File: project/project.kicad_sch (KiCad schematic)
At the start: 6 parts, among them J1 Conn_02x16_Odd_Even, J2 USB_C_Receptacle_PowerOnly_6P, SW1 SS-12D10L9, U2 CH224K

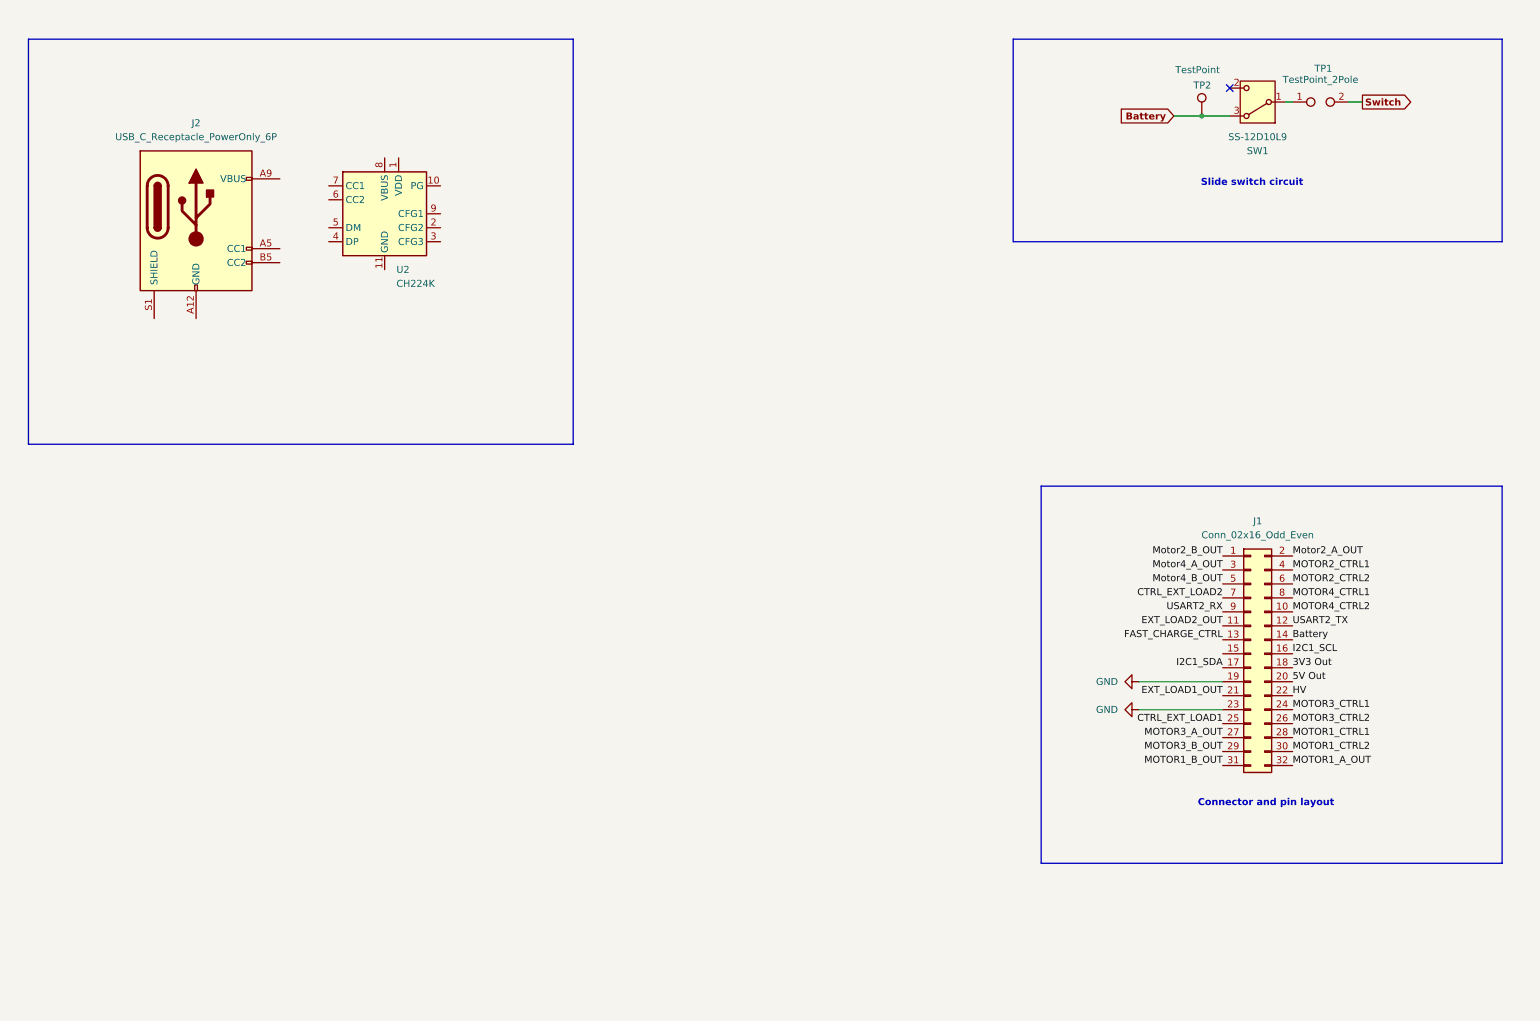
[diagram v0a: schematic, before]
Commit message: changed pull up resistor values
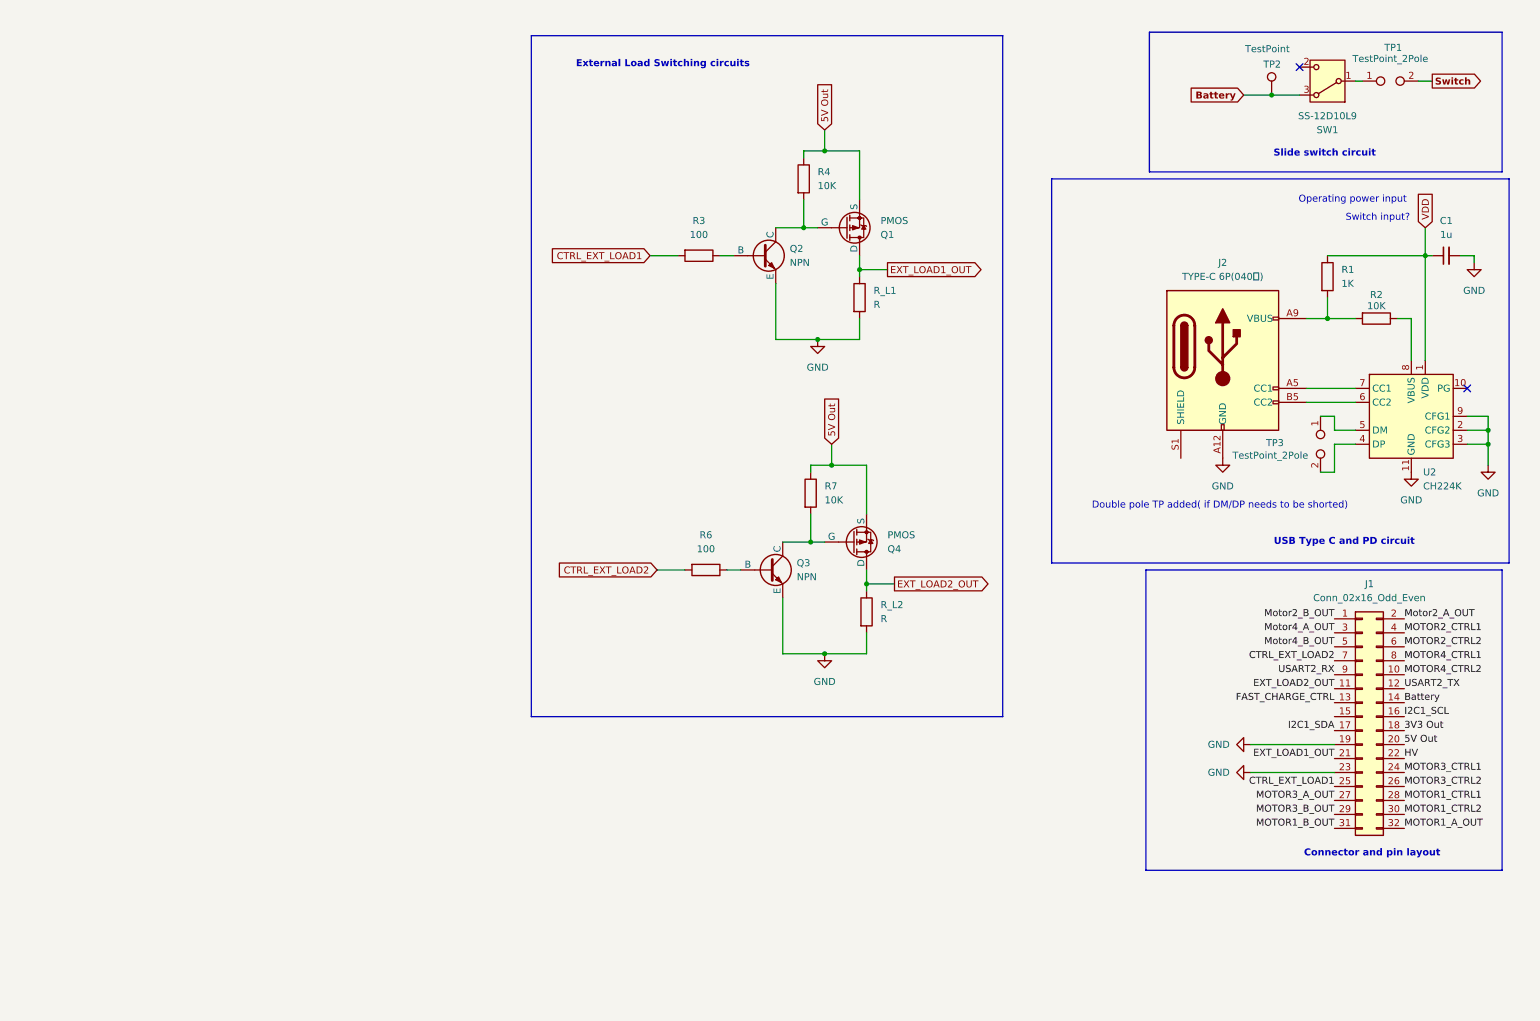
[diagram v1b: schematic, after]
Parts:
- added C1: 1u, symbol Device:C_Small
- added Q1, Q4: PMOS, symbol Simulation_SPICE:PMOS
- added Q2, Q3: NPN, symbol Simulation_SPICE:NPN
- added R1: 1K, symbol Device:R
- added R2, R4, R7: 10K, symbol Device:R
- added R3, R6: 100, symbol Device:R
- added R_L1, R_L2: R, symbol Device:R
- added TP3: TestPoint_2Pole, symbol Connector:TestPoint_2Pole
- J2: value USB_C_Receptacle_PowerOnly_6P -> TYPE-C 6P(040新)
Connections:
- net 5V Out: now also Q1.3 (S), Q4.3 (S), R4.1, R7.1
- net CTRL_EXT_LOAD1: now also R3.2
- net CTRL_EXT_LOAD2: now also R6.2
- net EXT_LOAD1_OUT: now also Q1.1 (D), R_L1.1
- net EXT_LOAD2_OUT: now also Q4.1 (D), R_L2.1
- net GND: now also J2.A12 (GND), J2.B12 (GND), U2.11 (GND), U2.2 (CFG2), U2.3 (CFG3), U2.9 (CFG1), C1.2, Q2.3 (E), Q3.3 (E), R_L1.2, R_L2.2
- net at J2.A5 (CC1): now also U2.7 (CC1)
- net at J2.A9 (VBUS), J2.B9 (VBUS): now also R1.2, R2.2
- net at J2.B5 (CC2): now also U2.6 (CC2)
- net VDD: now reaches U2.1 (VDD)
- net VDD: now also C1.1, R1.1
- net at U2.4 (DP): now also TP3.2
- net at U2.5 (DM): now also TP3.1
- net at U2.8 (VBUS): now also R2.1
- new net: Q1.2 (G), Q2.1 (C), R4.2
- new net: Q2.2 (B), R3.1
- new net: Q3.2 (B), R6.1
- new net: Q3.1 (C), Q4.2 (G), R7.2
- no-connect marks 1 -> 2
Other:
- note added: "Double pole TP added( if DM/DP needs to be shorted)"
- note added: "External Load Switching circuits"
- note added: "Operating power input"
- note added: "Switch input?"
- note added: "USB Type C and PD circuit"
- moved on the sheet: J1, J2, SW1, TP1, TP2, U2

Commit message: change resistor
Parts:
- R3: value 100 -> 200
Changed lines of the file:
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@@
 			)
 		)
-		(property "Value" "100"
+		(property "Value" "200"
 			(at 137.16 49.53 90)
 			(effects

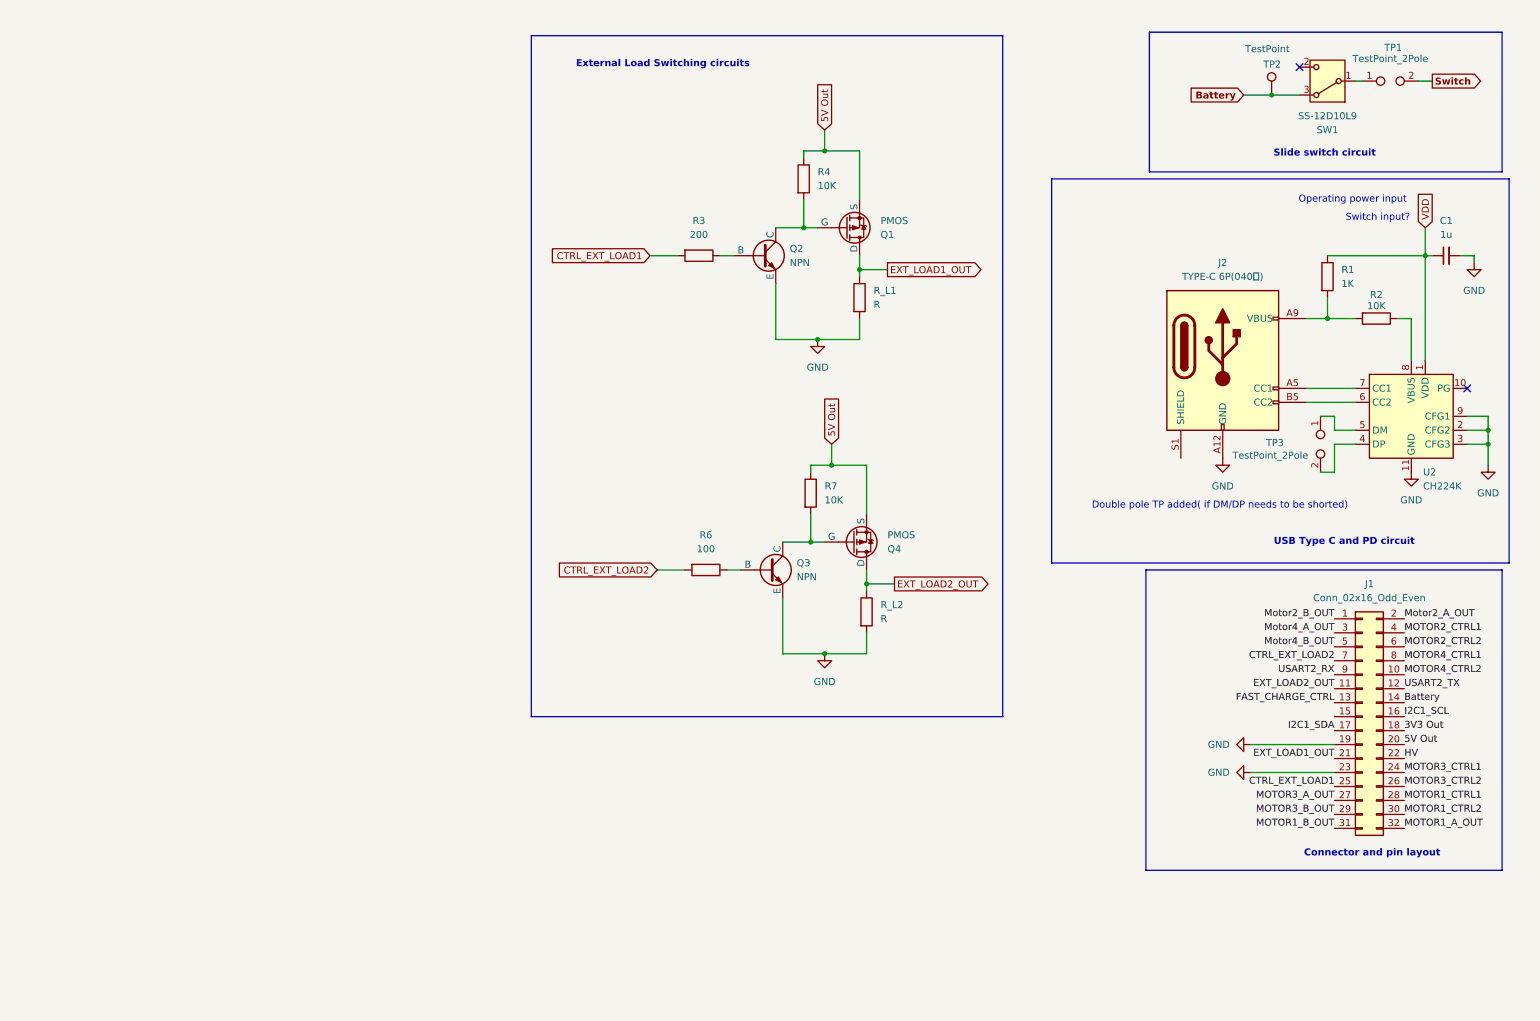
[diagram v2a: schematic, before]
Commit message: add Oxolo subsections
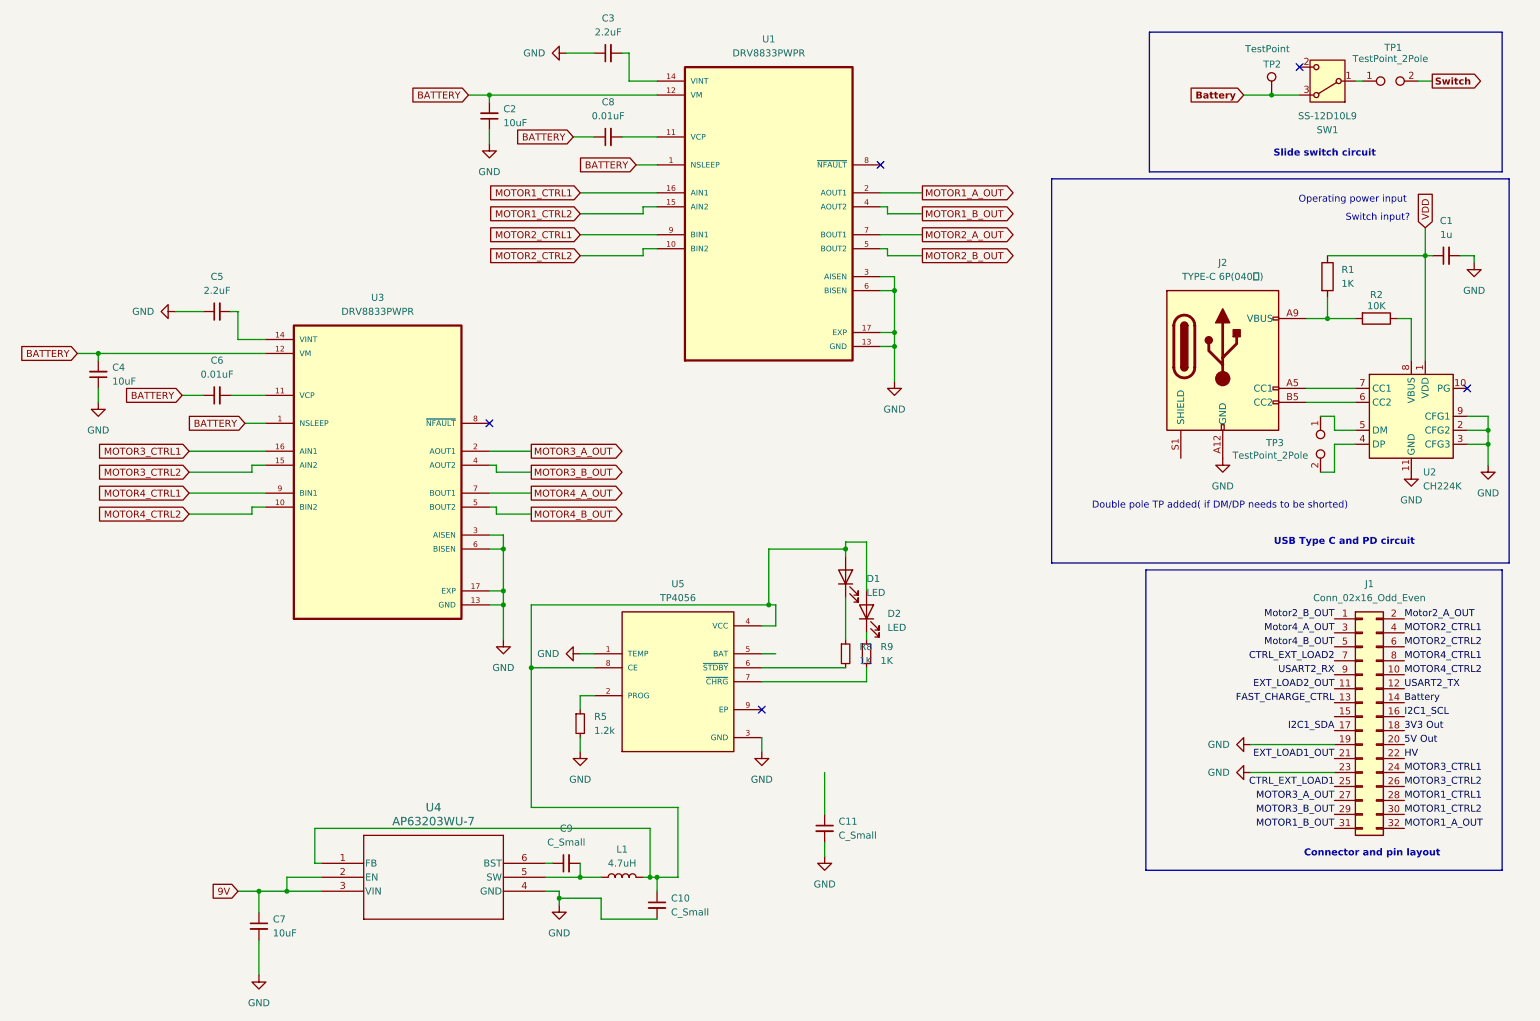
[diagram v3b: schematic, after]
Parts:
- removed Q1, Q4: PMOS, symbol Simulation_SPICE:PMOS
- removed Q2, Q3: NPN, symbol Simulation_SPICE:NPN
- removed R3: 200, symbol Device:R
- removed R4, R7: 10K, symbol Device:R
- removed R6: 100, symbol Device:R
- removed R_L1, R_L2: R, symbol Device:R
- added C10, C11, C9: C_Small, symbol Device:C_Small
- added C2, C4, C7: 10uF, symbol Device:C_Small
- added C3, C5: 2.2uF, symbol Device:C_Small
- added C6, C8: 0.01uF, symbol Device:C_Small
- added D1, D2: LED, symbol Device:LED
- added L1: 4.7uH, symbol Device:L
- added R5: 1.2k, symbol Device:R_Small
- added R8, R9: 1K, symbol Device:R_Small
- added U1, U3: DRV8833PWPR, DRV8833PWPR:IC_DRV8833PWPR, symbol DRV8833PWPR:DRV8833PWPR
- added U4: AP63203WU-7, AP63203WU-7_DIO, symbol AP63203WU-7:AP63203WU-7
- added U5: TP4056, TP4056:SOP127P600X175-9N, symbol TP4056:TP4056
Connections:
- net GND: now also C10.2, C11.2, C2.1, C3.1, C4.1, C5.1, C7.2, R5.2, U1.13 (GND), U1.17 (EXP), U1.3 (AISEN), U1.6 (BISEN), U3.13 (GND), U3.17 (EXP), U3.3 (AISEN), U3.6 (BISEN), U4.4 (GND), U5.1 (TEMP), U5.3 (GND)
- net MOTOR1_A_OUT: now also U1.2 (AOUT1)
- net MOTOR1_B_OUT: now also U1.4 (AOUT2)
- net MOTOR1_CTRL1: now also U1.16 (AIN1)
- net MOTOR1_CTRL2: now also U1.15 (AIN2)
- net MOTOR2_CTRL1: now also U1.9 (BIN1)
- net MOTOR2_CTRL2: now also U1.10 (BIN2)
- net MOTOR3_A_OUT: now also U3.2 (AOUT1)
- net MOTOR3_B_OUT: now also U3.4 (AOUT2)
- net MOTOR3_CTRL1: now also U3.16 (AIN1)
- net MOTOR3_CTRL2: now also U3.15 (AIN2)
- net MOTOR4_CTRL1: now also U3.9 (BIN1)
- net MOTOR4_CTRL2: now also U3.10 (BIN2)
- new net: R5.1, U5.2 (PROG)
- new net: C10.1, D1.2 (A), D2.2 (A), L1.2, U4.1 (FB), U5.4 (VCC), U5.8 (CE)
- new net: R8.2, U5.6 (~{STDBY})
- new net: R9.2, U5.7 (~{CHRG})
- new net: D1.1 (K), R8.1
- new net: C9.2, L1.1, U4.5 (SW)
- new net: C9.1, U4.6 (BST)
- new net: C6.2, U3.11 (VCP)
- new net: C5.2, U3.14 (VINT)
- new net: D2.1 (K), R9.1
- new net: C8.2, U1.11 (VCP)
- new net: C3.2, U1.14 (VINT)
- new net 9V: C7.1, U4.2 (EN), U4.3 (VIN)
- new net BATTERY: C2.2, C4.2, C6.1, C8.1, U1.1 (NSLEEP), U1.12 (VM), U3.1 (NSLEEP), U3.12 (VM)
- new net MOTOR2_A_OUT: U1.7 (BOUT1)
- new net MOTOR2_B_OUT: U1.5 (BOUT2)
- new net MOTOR4_A_OUT: U3.7 (BOUT1)
- new net MOTOR4_B_OUT: U3.5 (BOUT2)
- no-connect marks 2 -> 5
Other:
- note removed: "External Load Switching circuits"

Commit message: Rearranged.
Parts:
- removed C6: 0.01uF, symbol Device:C_Small
- added C12: 0.01uF, symbol Device:C_Small
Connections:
- net BATTERY: now also C12.1
- net MOTOR3_CTRL1: now also U3.9 (BIN1)
- net MOTOR3_CTRL2: now also U3.10 (BIN2)
- net MOTOR4_CTRL1: no longer U3.9 (BIN1)
- net MOTOR4_CTRL2: no longer U3.10 (BIN2)
- net at U3.11 (VCP): now also C12.2
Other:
- moved on the sheet: C10, C11, C2, C3, C7, C8, C9, D1, D2, L1, R5, R8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

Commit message: update
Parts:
- added C13, C6: 1uF, symbol Device:C_Small
- added J3: Conn_01x02_Pin, symbol Connector:Conn_01x02_Pin
- added R3, R4: 10K, symbol Device:R_Small
- added U6, U7: TPS22965DSGR, TPS22965DSGR:SON50P200X200X80-9N, symbol TPS22965DSGR:TPS22965DSGR
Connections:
- net CTRL_EXT_LOAD1: now also U6.3 (ON)
- net CTRL_EXT_LOAD2: now also U7.3 (ON)
- net EXT_LOAD1_OUT: now also R3.1, U6.7 (VOUT), U6.8 (VOUT)
- net EXT_LOAD2_OUT: now also R4.1, U7.7 (VOUT), U7.8 (VOUT)
- net GND: now also C13.2, C6.2, J3.2 (Pin_2), R3.2, R4.2, U6.5 (GND), U6.9 (GND), U6.9_1 (GND), U6.9_2 (GND), U7.5 (GND), U7.9 (GND), U7.9_1 (GND), U7.9_2 (GND)
- net BATT: now reaches U5.5 (BAT)
- net BATT: now also C11.1, J3.1 (Pin_1)
- new net 5V: C13.1, C6.1, U6.1 (VIN), U6.2 (VIN), U6.4 (VBIAS), U7.1 (VIN), U7.2 (VIN), U7.4 (VBIAS)
- no-connect marks 5 -> 7
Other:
- note added: "Motor drivers"
- note added: "Provide 2x External Load Switching at 1A each"
- note added: "The Charging circuit"

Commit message: changed batt
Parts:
- removed C13, C6: 1uF, symbol Device:C_Small
- removed J3: Conn_01x02_Pin, symbol Connector:Conn_01x02_Pin
- removed R3, R4: 10K, symbol Device:R_Small
- removed U6, U7: TPS22965DSGR, TPS22965DSGR:SON50P200X200X80-9N, symbol TPS22965DSGR:TPS22965DSGR
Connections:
- net Switch is gone; now on net Battery: TP1.2
- net Battery: no longer SW1.3 (A), TP2.1
- net BATT: no longer names the net of U5.5 (BAT)
- net BATT: no longer C11.1
- new net: SW1.3 (A), TP2.1
- no-connect marks 7 -> 5
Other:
- note removed: "Motor drivers"
- note removed: "Provide 2x External Load Switching at 1A each"
- note removed: "The Charging circuit"
